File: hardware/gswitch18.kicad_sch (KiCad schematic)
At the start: 26 parts

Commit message: MILESTONE: FIRST JLCPCB TEST ORDER
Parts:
- P1, P2, P3: JLCPCB C519164 -> C495552
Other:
- title: G9X USB Programmer -> USB 18 Button Game Controller
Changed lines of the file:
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@@
   (paper "A4")
   (title_block
-    (title "G9X USB Programmer")
-    (date "25 sep 2012")
-    (rev "1.1")
+    (title "USB 18 Button Game Controller")
+    (date "2022-04-28")
+    (rev "1.2")
   )
   (junction (at 50.8 142.24) (diameter 0) (color 0 0 0 0)
@@
       (effects (font (size 0.508 0.508)) hide)
     )
-    (property "Value" "" (id 1) (at 49.53 17.78 0)
+    (property "Value" "+5V" (id 1) (at 49.53 17.78 0)
       (effects (font (size 0.762 0.762)))
     )
@@
       (effects (font (size 0.762 0.762)) hide)
     )
-    (property "Value" "" (id 1) (at 38.1 64.008 0)
+    (property "Value" "GND" (id 1) (at 38.1 64.008 0)
       (effects (font (size 0.762 0.762)) hide)
     )
@@
       (effects (font (size 0.762 0.762)) hide)
     )
-    (property "Value" "" (id 1) (at 83.82 72.898 0)
+    (property "Value" "GND" (id 1) (at 83.82 72.898 0)
       (effects (font (size 0.762 0.762)) hide)
     )
@@
       (effects (font (size 0.762 0.762)) hide)
     )
-    (property "Value" "" (id 1) (at 92.71 72.898 0)
+    (property "Value" "GND" (id 1) (at 92.71 72.898 0)
       (effects (font (size 0.762 0.762)) hide)
     )
@@
       (effects (font (size 0.762 0.762)) hide)
     )
-    (property "Value" "" (id 1) (at 97.79 51.308 0)
+    (property "Value" "GND" (id 1) (at 97.79 51.308 0)
       (effects (font (size 0.762 0.762)) hide)
     )
@@
       (effects (font (size 0.762 0.762)) hide)
     )
-    (property "Value" "" (id 1) (at 106.68 51.308 0)
+    (property "Value" "GND" (id 1) (at 106.68 51.308 0)
       (effects (font (size 0.762 0.762)) hide)
     )
@@
       (effects (font (size 0.508 0.508)) hide)
     )
-    (property "Value" "" (id 1) (at 83.82 43.18 0)
+    (property "Value" "+5V" (id 1) (at 83.82 43.18 0)
       (effects (font (size 0.762 0.762)))
     )
@@
       (effects (font (size 0.762 0.762)) hide)
     )
-    (property "Value" "" (id 1) (at 50.8 104.648 0)
+    (property "Value" "GND" (id 1) (at 50.8 104.648 0)
       (effects (font (size 0.762 0.762)) hide)
     )
@@
       (effects (font (size 0.508 0.508)) hide)
     )
-    (property "Value" "" (id 1) (at 101.6 82.55 0)
+    (property "Value" "+5V" (id 1) (at 101.6 82.55 0)
       (effects (font (size 0.762 0.762)))
     )
@@
       (effects (font (size 0.762 0.762)) hide)
     )
-    (property "Value" "" (id 1) (at 102.87 173.228 0)
+    (property "Value" "GND" (id 1) (at 102.87 173.228 0)
       (effects (font (size 0.762 0.762)) hide)
     )
@@
       (effects (font (size 0.508 0.508)) hide)
     )
-    (property "Value" "" (id 1) (at 50.8 122.174 0)
+    (property "Value" "+5V" (id 1) (at 50.8 122.174 0)
       (effects (font (size 0.762 0.762)))
     )
@@
       (effects (font (size 0.762 0.762)) hide)
     )
-    (property "Value" "" (id 1) (at 73.66 170.688 0)
+    (property "Value" "GND" (id 1) (at 73.66 170.688 0)
       (effects (font (size 0.762 0.762)) hide)
     )
@@
       (effects (font (size 0.762 0.762)) hide)
     )
-    (property "Value" "" (id 1) (at 115.57 99.568 0)
+    (property "Value" "GND" (id 1) (at 115.57 99.568 0)
       (effects (font (size 0.762 0.762)) hide)
     )
@@
       (effects (font (size 0.508 0.508)) hide)
     )
-    (property "Value" "" (id 1) (at 50.8 77.47 0)
+    (property "Value" "+5V" (id 1) (at 50.8 77.47 0)
       (effects (font (size 0.762 0.762)))
     )
@@
       (effects (font (size 0.762 0.762)) hide)
     )
-    (property "Value" "" (id 1) (at 58.42 170.688 0)
+    (property "Value" "GND" (id 1) (at 58.42 170.688 0)
       (effects (font (size 0.762 0.762)) hide)
     )
@@
       (effects (font (size 0.762 0.762)) hide)
     )
-    (property "Value" "" (id 1) (at 87.63 100.838 0)
+    (property "Value" "GND" (id 1) (at 87.63 100.838 0)
       (effects (font (size 0.762 0.762)) hide)
     )
@@
       (effects (font (size 0.762 0.762)) hide)
     )
-    (property "Value" "" (id 1) (at 71.12 155.448 0)
+    (property "Value" "GND" (id 1) (at 71.12 155.448 0)
       (effects (font (size 0.762 0.762)) hide)
     )
@@
       (effects (font (size 0.762 0.762)) hide)
     )
-    (property "Value" "" (id 1) (at 66.04 166.878 0)
+    (property "Value" "GND" (id 1) (at 66.04 166.878 0)
       (effects (font (size 0.762 0.762)) hide)
     )
@@
       (effects (font (size 1.27 1.27)) hide)
     )
-    (property "JLCPCB" "C519164" (id 4) (at 165.1 102.87 0)
+    (property "JLCPCB" "C495552" (id 4) (at 165.1 102.87 0)
       (effects (font (size 1.27 1.27)) hide)
     )
@@
       (effects (font (size 0.762 0.762)) hide)
     )
-    (property "Value" "" (id 1) (at 157.48 144.018 0)
+    (property "Value" "GND" (id 1) (at 157.48 144.018 0)
       (effects (font (size 0.762 0.762)) hide)
     )
@@
       (effects (font (size 1.27 1.27)) hide)
     )
-    (property "JLCPCB" "C519164" (id 4) (at 165.1 76.2 0)
+    (property "JLCPCB" "C495552" (id 4) (at 165.1 76.2 0)
       (effects (font (size 1.27 1.27)) hide)
     )
@@
       (effects (font (size 0.762 0.762)) hide)
     )
-    (property "Value" "" (id 1) (at 157.48 116.078 0)
+    (property "Value" "GND" (id 1) (at 157.48 116.078 0)
       (effects (font (size 0.762 0.762)) hide)
     )
@@
       (effects (font (size 0.762 0.762)) hide)
     )
-    (property "Value" "" (id 1) (at 55.88 39.878 0)
+    (property "Value" "GND" (id 1) (at 55.88 39.878 0)
       (effects (font (size 0.762 0.762)) hide)
     )
@@
       (effects (font (size 1.27 1.27)) hide)
     )
-    (property "JLCPCB" "C519164" (id 4) (at 165.1 130.81 0)
+    (property "JLCPCB" "C495552" (id 4) (at 165.1 130.81 0)
       (effects (font (size 1.27 1.27)) hide)
     )
@@
       (effects (font (size 0.762 0.762)) hide)
     )
-    (property "Value" "" (id 1) (at 157.48 89.408 0)
+    (property "Value" "GND" (id 1) (at 157.48 89.408 0)
       (effects (font (size 0.762 0.762)) hide)
     )
@@
       (effects (font (size 0.762 0.762)) hide)
     )
-    (property "Value" "" (id 1) (at 153.67 189.738 0)
-      (effects (font (size 0.762 0.762)) hide)
-    )
+    (property "Value" "GND" (id 1) (at 153.67 189.738 0)
+      (effects (font (size 0.762 0.762)) hide)
+    )

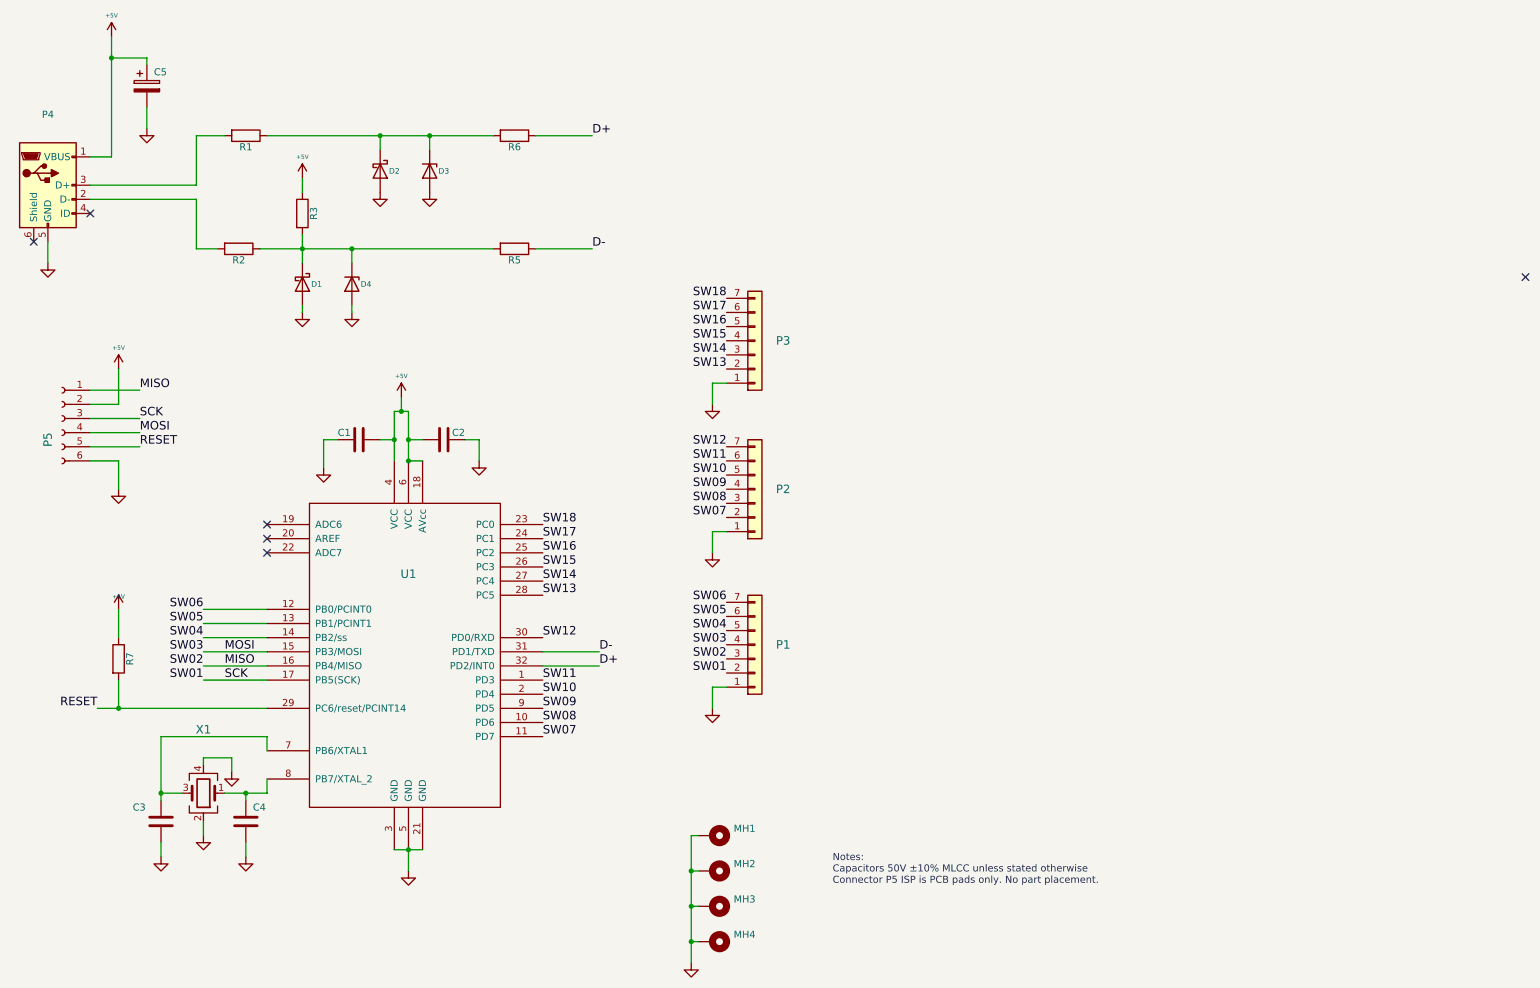
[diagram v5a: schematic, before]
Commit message: Schematic tidy-up (wasting time because why not?)
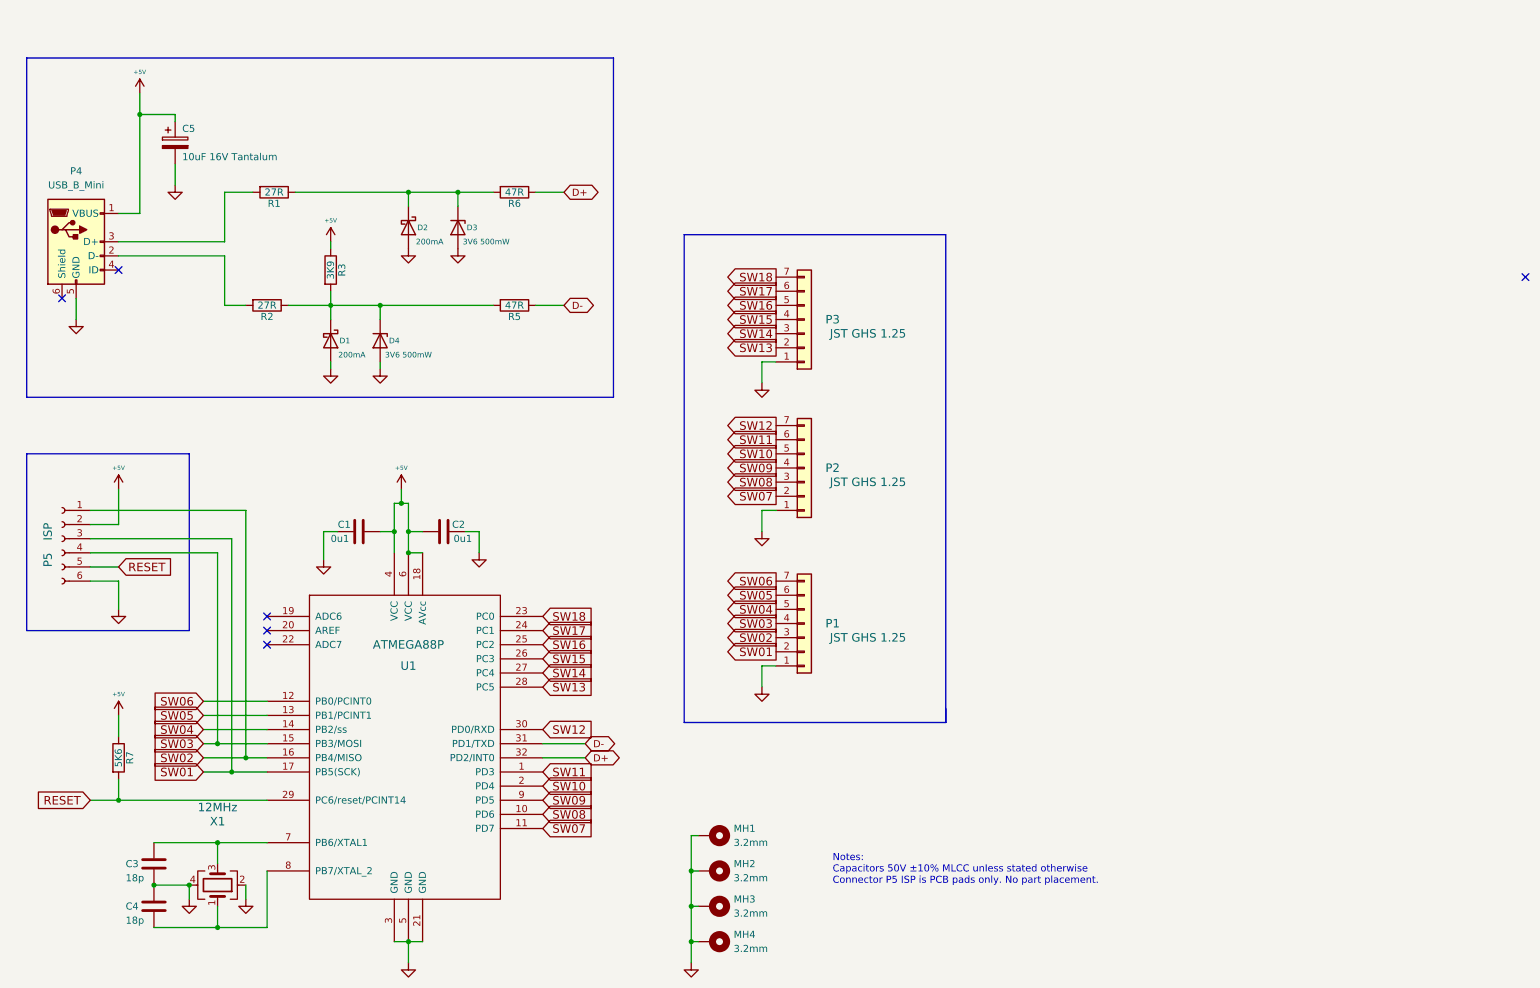
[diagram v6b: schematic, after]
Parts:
- C1, C2: value (none) -> 0u1; footprint (none) -> Capacitor_SMD:C_0603_1608Metric
- C3, C4: value (none) -> 18p; footprint (none) -> Capacitor_SMD:C_0603_1608Metric
- C5: value (none) -> 10uF 16V Tantalum; footprint (none) -> Capacitor_SMD:C_1206_3216Metric
- D1, D2: value (none) -> 200mA; footprint (none) -> Diode_SMD:D_SOD-523
- D3, D4: value (none) -> 3V6 500mW; footprint (none) -> Diode_SMD:D_SOD-123
- MH1, MH2, MH3, MH4: value (none) -> 3.2mm
- P1, P2, P3: value (none) -> JST GHS 1.25; footprint (none) -> Connector_JST:JST_GH_BM07B-GHS-TBT_1x07-1MP_P1.25mm_Vertical
- P4: value (none) -> USB_B_Mini; footprint (none) -> Connector_USB:USB_Mini-B_Wuerth_65100516121_Horizontal
- P5: value (none) -> ISP; footprint (none) -> Connector_PinHeader_2.54mm:PinHeader_2x03_P2.54mm_Vertical
- R1, R2: value (none) -> 27R; footprint (none) -> Resistor_SMD:R_0603_1608Metric
- R3: value (none) -> 3K9; footprint (none) -> Resistor_SMD:R_0603_1608Metric
- R5, R6: value (none) -> 47R; footprint (none) -> Resistor_SMD:R_0603_1608Metric
- R7: value (none) -> 5K6; footprint (none) -> Resistor_SMD:R_0603_1608Metric
- U1: value (none) -> ATMEGA88P; footprint (none) -> Package_QFP:TQFP-32_7x7mm_P0.8mm
- X1: value (none) -> 12MHz; footprint (none) -> Crystal:Crystal_SMD_3225-4Pin_3.2x2.5mm
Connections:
- net GND: now also C4.1; no longer C4.2
- net at U1.8 (PB7/XTAL_2), X1.1: now also C4.2; no longer C4.1
- net MISO renamed SW02
- net MOSI renamed SW03
- net SCK renamed SW01
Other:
- moved on the sheet: C1, C2, C3, C4, C5, D1, D2, D3, D4, P1, P2, P3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
